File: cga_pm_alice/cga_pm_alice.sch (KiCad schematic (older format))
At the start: 197 parts, among them J1 MX-LED, K1 MX-LED, M1 MX-LED, P1 MX-LED, Q1 MX-LED, SW1 reset_button, T1 MX-LED, U1 MX-LED, X1 MX-LED, Y1 MX-LED, m1 MX-LED, m2 MX-LED

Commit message: Another botchy attempt
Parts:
- renumbered s`1 to sQT1
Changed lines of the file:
@@
 	800  2950 800  3000
 $Comp
-L MX_Alps_Hybrid:MX-LED s`1
+L MX_Alps_Hybrid:MX-LED sQT1
 U 1 1 602E1642
 P 1100 2800
-F 0 "s`1" H 1182 3024 60  0000 C CNN
+F 0 "sQT1" H 1182 3024 60  0000 C CNN
 F 1 "MX-LED" H 1182 2950 20  0000 C CNN
 F 2 "Keebio-Parts:MX-Alps-Choc-1U" H 475 2775 60  0001 C CNN

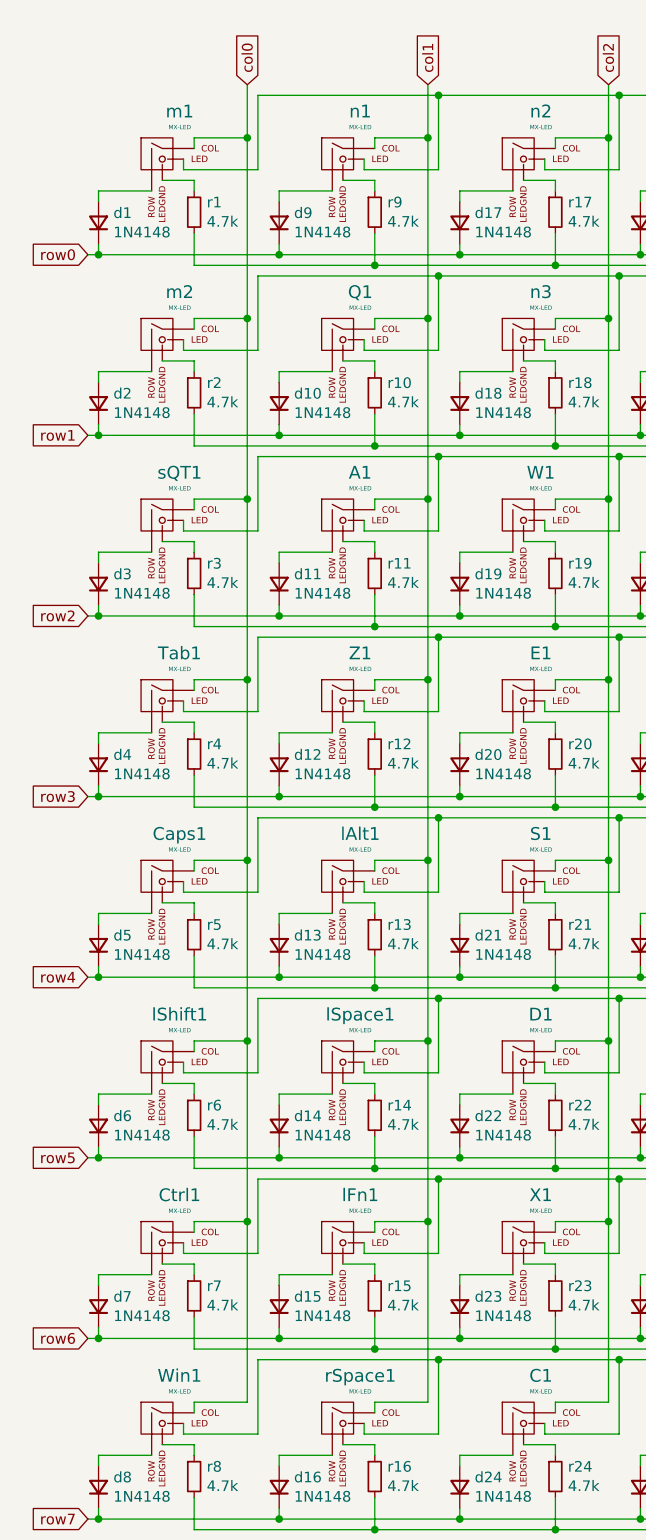
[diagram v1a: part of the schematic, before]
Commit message: Update cga_pm_alice files to linux
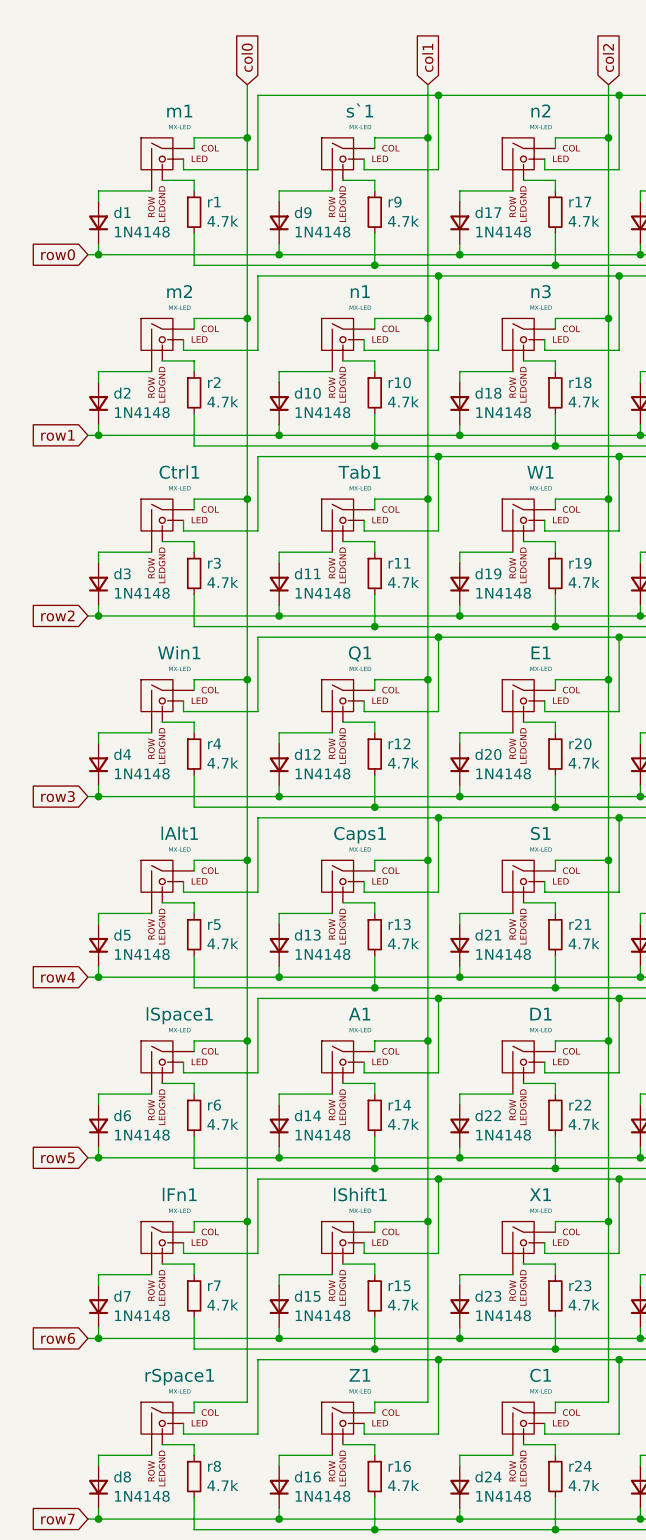
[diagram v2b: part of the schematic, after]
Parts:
- d1, d10, d11, d12, d13, d14, d15, d16, d17, d18, d19, d2, d20, d21, d22, d23, d24, d25, d26, d27, d28, d29, d3, d30, d31, d32, d33, d34, d35, d36, d37, d38, d39, d4, d40, d41, d42, d43, d44, d45, d46, d47, d48, d49, d5, d50, d51, d52, d53, d54, d55, d56, d57, d58, d59, d6, d60, d61, d62, d63, d64, d7, d8, d9: footprint Keebio-Parts:Diode-dual -> Keebio-Parts:Diode_Long
- r1, r10, r11, r12, r13, r14, r15, r16, r17, r18, r19, r2, r20, r21, r22, r23, r24, r25, r26, r27, r28, r29, r3, r30, r31, r32, r33, r34, r35, r36, r37, r38, r39, r4, r40, r41, r42, r43, r44, r45, r46, r47, r48, r49, r5, r50, r51, r52, r53, r54, r55, r56, r57, r58, r59, r6, r60, r61, r62, r63, r64, r7, r8, r9: footprint Keebio-Parts:Resistor-Hybrid -> Keebio-Parts:Resistor
- renumbered sQT1 to s`1
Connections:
- net col0: now also lAlt1.1 (COL), lFn1.1 (COL), lSpace1.1 (COL), rSpace1.1 (COL); no longer Caps1.1 (COL), Tab1.1 (COL), lShift1.1 (COL), s`1.1 (COL)
- net col1: now also Caps1.1 (COL), Tab1.1 (COL), lShift1.1 (COL), s`1.1 (COL); no longer lAlt1.1 (COL), lFn1.1 (COL), lSpace1.1 (COL), rSpace1.1 (COL)
- net at n1.2 (ROW): now also d10.2 (A); no longer d9.2 (A)
- net at n1.4 (LEDGND): now also r10.1; no longer r9.1
- net at Q1.2 (ROW): now also d12.2 (A); no longer d10.2 (A)
- net at Q1.4 (LEDGND): now also r12.1; no longer r10.1
- net at A1.2 (ROW): now also d14.2 (A); no longer d11.2 (A)
- net at A1.4 (LEDGND): now also r14.1; no longer r11.1
- net at s`1.2 (ROW): now also d9.2 (A); no longer d3.2 (A)
- net at s`1.4 (LEDGND): now also r9.1; no longer r3.1
- net at Z1.2 (ROW): now also d16.2 (A); no longer d12.2 (A)
- net at Z1.4 (LEDGND): now also r16.1; no longer r12.1
- net at Tab1.2 (ROW): now also d11.2 (A); no longer d4.2 (A)
- net at Tab1.4 (LEDGND): now also r11.1; no longer r4.1
- net at lAlt1.2 (ROW): now also d5.2 (A); no longer d13.2 (A)
- net at lAlt1.4 (LEDGND): now also r5.1; no longer r13.1
- net at Caps1.2 (ROW): now also d13.2 (A); no longer d5.2 (A)
- net at Caps1.4 (LEDGND): now also r13.1; no longer r5.1
- net at lSpace1.2 (ROW): now also d6.2 (A); no longer d14.2 (A)
- net at lSpace1.4 (LEDGND): now also r6.1; no longer r14.1
- net at lShift1.2 (ROW): now also d15.2 (A); no longer d6.2 (A)
- net at lShift1.4 (LEDGND): now also r15.1; no longer r6.1
- net at lFn1.2 (ROW): now also d7.2 (A); no longer d15.2 (A)
- net at lFn1.4 (LEDGND): now also r7.1; no longer r15.1
- net at Ctrl1.2 (ROW): now also d3.2 (A); no longer d7.2 (A)
- net at Ctrl1.4 (LEDGND): now also r3.1; no longer r7.1
- net at rSpace1.2 (ROW): now also d8.2 (A); no longer d16.2 (A)
- net at rSpace1.4 (LEDGND): now also r8.1; no longer r16.1
- net at Win1.2 (ROW): now also d4.2 (A); no longer d8.2 (A)
- net at Win1.4 (LEDGND): now also r4.1; no longer r8.1
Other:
- moved on the sheet: A1, Caps1, Ctrl1, Q1, Tab1, Win1, Z1, lAlt1, lFn1, lShift1, lSpace1, n1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
